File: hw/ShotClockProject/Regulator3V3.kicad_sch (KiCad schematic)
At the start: 10 parts, among them U2 TPS63000

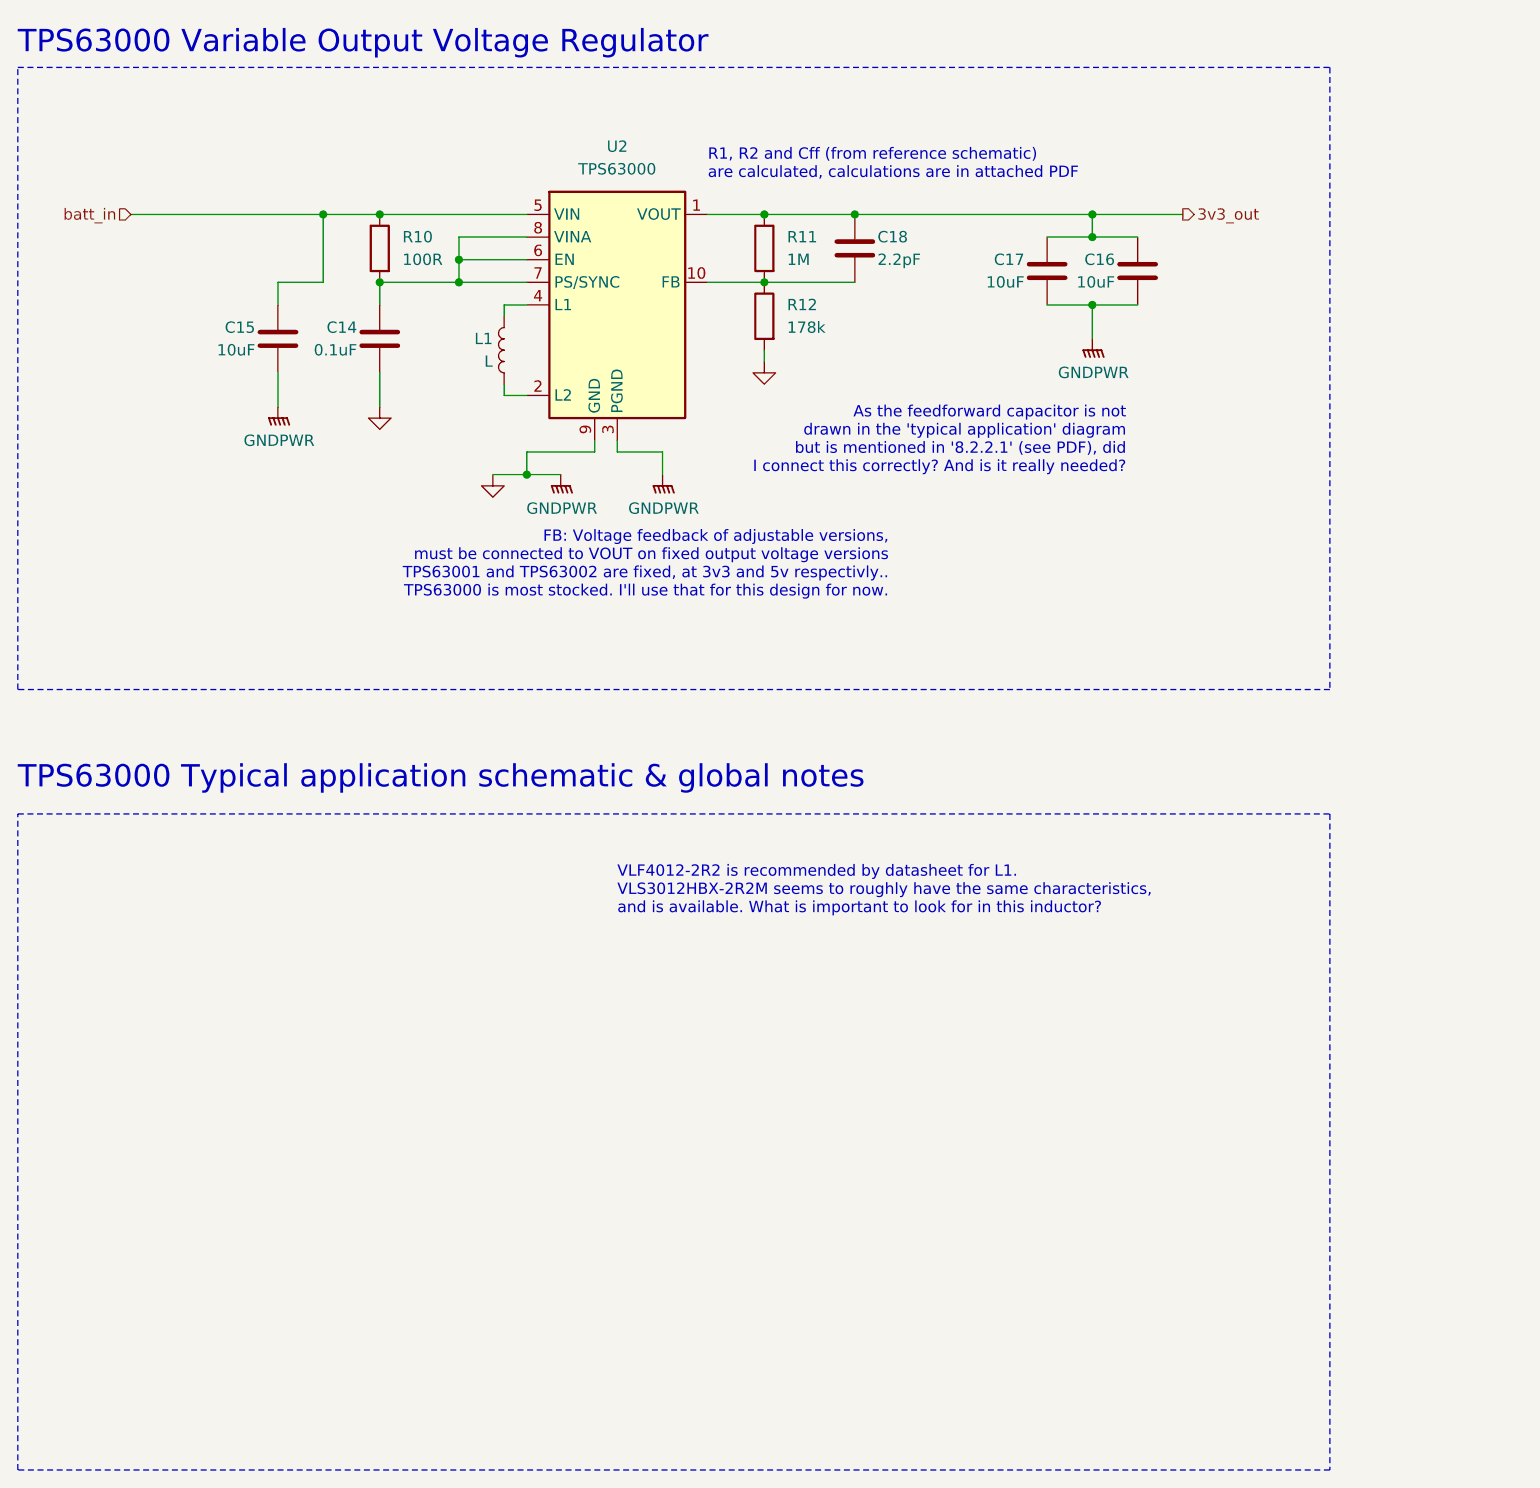
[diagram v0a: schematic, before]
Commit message: Fixed all ERC issues
Mainly by placing PWR_FLAGs and NetTies to show KiCAD where the GNDs are connected to each other physically, without them being the same net.
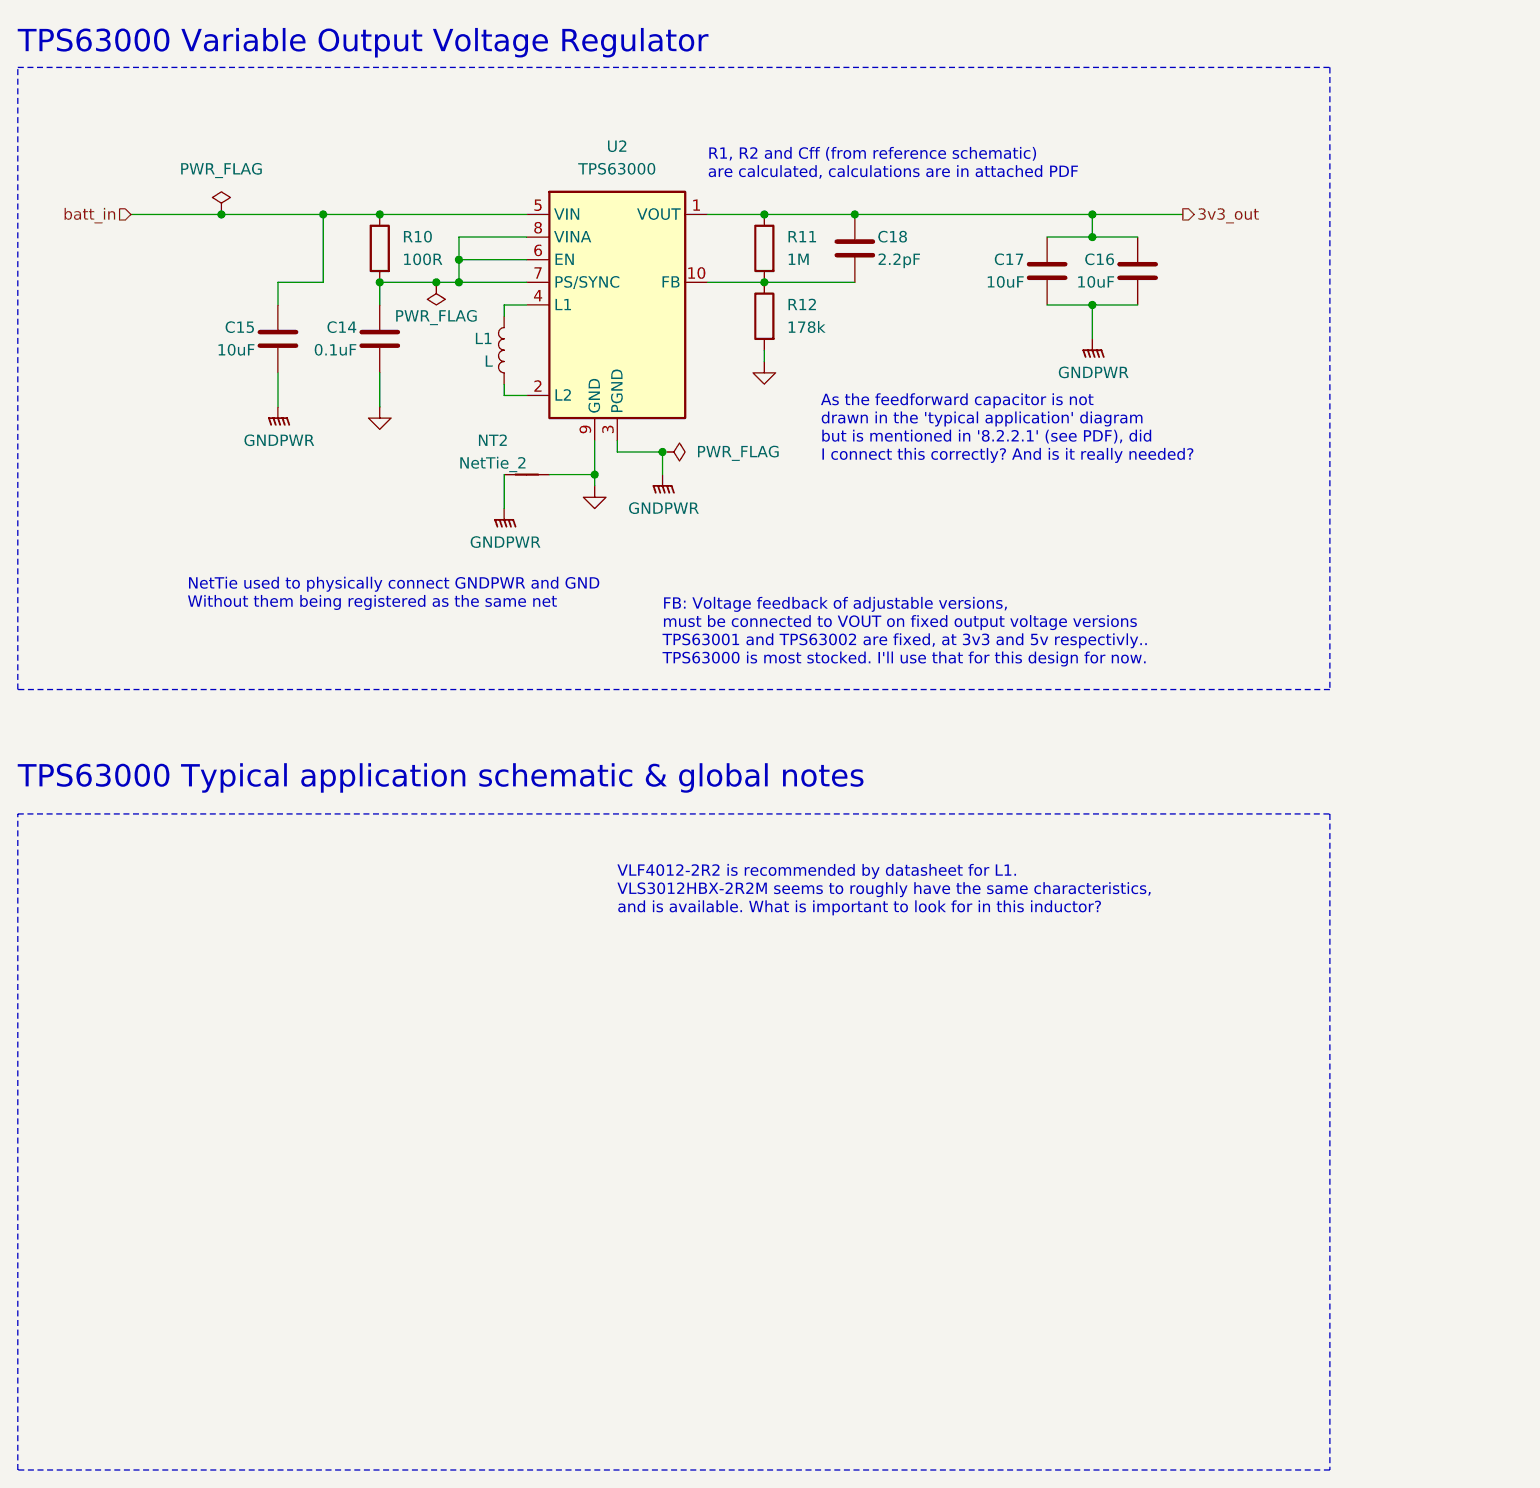
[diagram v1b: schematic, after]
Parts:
- added NT2: NetTie_2, symbol Device:NetTie_2
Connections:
- net GND: now also NT2.2; no longer C15.2, C16.2, C17.2, U2.11 (PGND), U2.3 (PGND)
- new net GNDPWR: C15.2, C16.2, C17.2, NT2.1, U2.11 (PGND), U2.3 (PGND)
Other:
- note added: "NetTie used to physically connect GNDPWR and GND Without them being registered as the same net"

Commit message: Init of SW, changes on HW
SW init STMIDE project
HW Added first few footprints for passive components.
Removed old name .IOC file
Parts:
- C14, C16, C17, C18: footprint (none) -> Capacitor_SMD:C_0402_1005Metric
- C15: footprint (none) -> Capacitor_SMD:C_0603_1608Metric
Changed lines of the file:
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@@
       (effects (font (size 1.27 1.27)) (justify left))
     )
-    (property "Footprint" "" (at 143.8148 48.26 0)
+    (property "Footprint" "Capacitor_SMD:C_0402_1005Metric" (at 143.8148 48.26 0)
       (effects (font (size 1.27 1.27)) hide)
     )
@@
       (effects (font (size 1.27 1.27)) (justify left))
     )
-    (property "Footprint" "" (at 58.7248 55.88 0)
+    (property "Footprint" "Capacitor_SMD:C_0402_1005Metric" (at 58.7248 55.88 0)
       (effects (font (size 1.27 1.27)) hide)
     )
@@
       (effects (font (size 1.27 1.27)) (justify left))
     )
-    (property "Footprint" "" (at 47.2948 55.88 0)
+    (property "Footprint" "Capacitor_SMD:C_0603_1608Metric" (at 47.2948 55.88 0)
       (effects (font (size 1.27 1.27)) hide)
     )
@@
       (effects (font (size 1.27 1.27)) (justify left))
     )
-    (property "Footprint" "" (at 133.6548 48.26 0)
+    (property "Footprint" "Capacitor_SMD:C_0402_1005Metric" (at 133.6548 48.26 0)
       (effects (font (size 1.27 1.27)) hide)
     )
@@
       (effects (font (size 1.27 1.27)) (justify left))
     )
-    (property "Footprint" "" (at 113.9952 45.72 0)
-      (effects (font (size 1.27 1.27)) hide)
-    )
+    (property "Footprint" "Capacitor_SMD:C_0402_1005Metric" (at 113.9952 45.72 0)
+      (effects (font (size 1.27 1.27)) hide)
+    )

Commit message: Finished footprint selection & updated design doc
Chosen all footprints
Updated design doc with part link & part selection reasons
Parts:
- C14: value 0.1uF -> 0.1u; footprint Capacitor_SMD:C_0402_1005Metric -> Capacitor_SMD:C_0603_1608Metric
- C15: value 10uF -> 10u
- C16, C17: value 10uF -> 10u; footprint Capacitor_SMD:C_0402_1005Metric -> Capacitor_SMD:C_0603_1608Metric
- C18: value 2.2pF -> 2.2p; footprint Capacitor_SMD:C_0402_1005Metric -> Capacitor_SMD:C_0603_1608Metric
- L1: footprint (none) -> Inductor_SMD:L_Sunlord_SWPA3012S
- NT2: footprint (none) -> NetTie:NetTie-2_SMD_Pad2.0mm
- R10, R11, R12: footprint (none) -> Resistor_SMD:R_0603_1608Metric
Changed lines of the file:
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@@
       (effects (font (size 1.27 1.27)) (justify left))
     )
-    (property "Value" "10uF" (at 142.24 45.72 0)
-      (effects (font (size 1.27 1.27)) (justify left))
-    )
-    (property "Footprint" "Capacitor_SMD:C_0402_1005Metric" (at 143.8148 48.26 0)
+    (property "Value" "10u" (at 142.24 45.72 0)
+      (effects (font (size 1.27 1.27)) (justify left))
+    )
+    (property "Footprint" "Capacitor_SMD:C_0603_1608Metric" (at 143.8148 48.26 0)
       (effects (font (size 1.27 1.27)) hide)
     )
@@
       (effects (font (size 1.27 1.27)) (justify left))
     )
-    (property "Value" "0.1uF" (at 57.15 53.34 0)
-      (effects (font (size 1.27 1.27)) (justify left))
-    )
-    (property "Footprint" "Capacitor_SMD:C_0402_1005Metric" (at 58.7248 55.88 0)
+    (property "Value" "0.1u" (at 57.15 53.34 0)
+      (effects (font (size 1.27 1.27)) (justify left))
+    )
+    (property "Footprint" "Capacitor_SMD:C_0603_1608Metric" (at 58.7248 55.88 0)
       (effects (font (size 1.27 1.27)) hide)
     )
@@
       (effects (font (size 1.27 1.27)) (justify right))
     )
-    (property "Footprint" "" (at 104.648 41.91 90)
+    (property "Footprint" "Resistor_SMD:R_0603_1608Metric" (at 104.648 41.91 90)
       (effects (font (size 1.27 1.27)) hide)
     )
@@
       (effects (font (size 1.27 1.27)) (justify left))
     )
-    (property "Value" "10uF" (at 45.72 53.34 0)
+    (property "Value" "10u" (at 45.72 53.34 0)
       (effects (font (size 1.27 1.27)) (justify left))
     )
@@
       (effects (font (size 1.27 1.27)) (justify left))
     )
-    (property "Value" "10uF" (at 132.08 45.72 0)
-      (effects (font (size 1.27 1.27)) (justify left))
-    )
-    (property "Footprint" "Capacitor_SMD:C_0402_1005Metric" (at 133.6548 48.26 0)
+    (property "Value" "10u" (at 132.08 45.72 0)
+      (effects (font (size 1.27 1.27)) (justify left))
+    )
+    (property "Footprint" "Capacitor_SMD:C_0603_1608Metric" (at 133.6548 48.26 0)
       (effects (font (size 1.27 1.27)) hide)
     )
@@
       (effects (font (size 1.27 1.27)) (justify right))
     )
-    (property "Footprint" "" (at 104.648 49.53 90)
+    (property "Footprint" "Resistor_SMD:R_0603_1608Metric" (at 104.648 49.53 90)
       (effects (font (size 1.27 1.27)) hide)
     )
@@
       (effects (font (size 1.27 1.27)))
     )
-    (property "Footprint" "" (at 76.2 67.31 0)
+    (property "Footprint" "NetTie:NetTie-2_SMD_Pad2.0mm" (at 76.2 67.31 0)
       (effects (font (size 1.27 1.27)) hide)
     )
@@
       (effects (font (size 1.27 1.27)) (justify left))
     )
-    (property "Value" "2.2pF" (at 115.57 43.18 0)
-      (effects (font (size 1.27 1.27)) (justify left))
-    )
-    (property "Footprint" "Capacitor_SMD:C_0402_1005Metric" (at 113.9952 45.72 0)
+    (property "Value" "2.2p" (at 115.57 43.18 0)
+      (effects (font (size 1.27 1.27)) (justify left))
+    )
+    (property "Footprint" "Capacitor_SMD:C_0603_1608Metric" (at 113.9952 45.72 0)
       (effects (font (size 1.27 1.27)) hide)
     )
@@
       (effects (font (size 1.27 1.27)) (justify right))
     )
-    (property "Footprint" "" (at 61.468 41.91 90)
+    (property "Footprint" "Resistor_SMD:R_0603_1608Metric" (at 61.468 41.91 90)
       (effects (font (size 1.27 1.27)) hide)
     )
@@
       (effects (font (size 1.27 1.27)) (justify left))
     )
-    (property "Footprint" "" (at 73.66 53.34 0)
-      (effects (font (size 1.27 1.27)) hide)
-    )
+    (property "Footprint" "Inductor_SMD:L_Sunlord_SWPA3012S" (at 73.66 53.34 0)
+      (effects (font (size 1.27 1.27)) hide)
+    )

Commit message: Changed footprint
To horizontal 2.54 connectors
and started on rough layout
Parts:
- C14, C18: footprint Capacitor_SMD:C_0603_1608Metric -> Capacitor_SMD:C_0402_1005Metric
- R10, R11, R12: footprint Resistor_SMD:R_0603_1608Metric -> Resistor_SMD:R_0402_1005Metric
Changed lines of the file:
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@@
       (effects (font (size 1.27 1.27)) (justify left))
     )
-    (property "Footprint" "Capacitor_SMD:C_0603_1608Metric" (at 58.7248 55.88 0)
+    (property "Footprint" "Capacitor_SMD:C_0402_1005Metric" (at 58.7248 55.88 0)
       (effects (font (size 1.27 1.27)) hide)
     )
@@
       (effects (font (size 1.27 1.27)) (justify right))
     )
-    (property "Footprint" "Resistor_SMD:R_0603_1608Metric" (at 104.648 41.91 90)
+    (property "Footprint" "Resistor_SMD:R_0402_1005Metric" (at 104.648 41.91 90)
       (effects (font (size 1.27 1.27)) hide)
     )
@@
       (effects (font (size 1.27 1.27)) (justify right))
     )
-    (property "Footprint" "Resistor_SMD:R_0603_1608Metric" (at 104.648 49.53 90)
+    (property "Footprint" "Resistor_SMD:R_0402_1005Metric" (at 104.648 49.53 90)
       (effects (font (size 1.27 1.27)) hide)
     )
@@
       (effects (font (size 1.27 1.27)) (justify left))
     )
-    (property "Footprint" "Capacitor_SMD:C_0603_1608Metric" (at 113.9952 45.72 0)
+    (property "Footprint" "Capacitor_SMD:C_0402_1005Metric" (at 113.9952 45.72 0)
       (effects (font (size 1.27 1.27)) hide)
     )
@@
       (effects (font (size 1.27 1.27)) (justify right))
     )
-    (property "Footprint" "Resistor_SMD:R_0603_1608Metric" (at 61.468 41.91 90)
-      (effects (font (size 1.27 1.27)) hide)
-    )
+    (property "Footprint" "Resistor_SMD:R_0402_1005Metric" (at 61.468 41.91 90)
+      (effects (font (size 1.27 1.27)) hide)
+    )
